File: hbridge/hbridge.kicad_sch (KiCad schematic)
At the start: 81 parts, among them J1 From_MCU, J10 From_MCU, J11 MOSFET_out, J12 Conn_01x03, J13 Conn_01x01_Socket, J14 Conn_01x01_Socket, J15 VEE connector, J16 VEE connector, J17 VEE connector, J18 VEE connector, J2 MOSFET_out, J3 Conn_01x03, J4 From_MCU, J5 MOSFET_out, J6 Conn_01x03, J7 From_MCU, J8 MOSFET_out, J9 Conn_01x03, Q1 IRF3710, Q2 IRF3710, Q3 IRF3710, Q4 IRF3710, U1 LDO-3.3, U5 NSi6651A, U6 NSi6651A, U7 NSi6651A, U8 NSi6651A

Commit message: Half bridge power to PCB added.
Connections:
- net GND_DRV2: no longer J12.2 (Pin_2), J15.1 (Pin_1), J16.1 (Pin_1), J17.1 (Pin_1), J18.1 (Pin_1), J3.2 (Pin_2), J6.2 (Pin_2), J9.2 (Pin_2)
- net +12V: now reaches C3.1, J13.1 (Pin_1), U1.1 (IN)
- net +15_DRV2 renamed +15_DRV2_H
- net +15_DRV2_H: no longer C4.2, C6.2, J12.1 (Pin_1), J6.1 (Pin_1), U6.5 (VCC2), U8.5 (VCC2)
- net -15_DRV2 renamed -15_DRV2_H
- net -15_DRV2_H: no longer J12.3 (Pin_3), J16.3 (Pin_3), J18.3 (Pin_3), J6.3 (Pin_3)
- new net +15_DRV2_L: C4.2, C6.2, J12.1 (Pin_1), J6.1 (Pin_1), U6.5 (VCC2), U8.5 (VCC2)
- new net -15_DRV2_L: J12.3 (Pin_3), J16.3 (Pin_3), J18.3 (Pin_3), J6.3 (Pin_3)
- new net GND_DRV2_H: J15.1 (Pin_1), J17.1 (Pin_1), J3.2 (Pin_2), J9.2 (Pin_2)
- new net GND_DRV2_L: J12.2 (Pin_2), J16.1 (Pin_1), J18.1 (Pin_1), J6.2 (Pin_2)
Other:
- note added: "? мб нужна логика защиты полумоста от мертвого времени и тд?"
- note added: "Q1"
- note added: "Q2"
- note added: "Q3"
- note added: "Q4"
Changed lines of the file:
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@@
 	(generator_version "10.0")
 	(paper "A3")
+	(text "Q1"
+		(exclude_from_sim no)
+		(at 169.418 86.106 0)
+		(effects
+			(font
+				(size 1.27 1.27)
+			)
+		)
+	)
+	(text "Q4"
+		(exclude_from_sim no)
+		(at 358.394 222.758 0)
+		(effects
+			(font
+				(size 1.27 1.27)
+			)
+		)
+	)
+	(text "Q2"
+		(exclude_from_sim no)
+		(at 385.826 102.108 0)
+		(effects
+			(font
+				(size 1.27 1.27)
+			)
+		)
+	)
+	(text "? мб нужна логика защиты полумоста от мертвого времени и тд?"
+		(exclude_from_sim no)
+		(at 72.644 257.302 0)
+		(effects
+			(font
+				(size 1.27 1.27)
+			)
+		)
+	)
+	(text "Q3"
+		(exclude_from_sim no)
+		(at 152.146 186.944 0)
+		(effects
+			(font
+				(size 1.27 1.27)
+			)
+		)
+	)
 	(junction
 		(at 247.65 190.5)
@@
 	)
 	(junction
+		(at 252.73 26.67)
+		(diameter 0)
+		(color 0 0 0 0)
+	)
+	(junction
 		(at 288.29 222.25)
 		(diameter 0)
@@
 	(wire
 		(pts
+			(xy 264.16 25.4) (xy 264.16 26.67)
+		)
+		(stroke
+			(width 0)
+			(type default)
+		)
+	)
+	(wire
+		(pts
 			(xy 257.81 193.04) (xy 257.81 198.12)
 		)
@@
 	(wire
 		(pts
+			(xy 252.73 26.67) (xy 264.16 26.67)
+		)
+		(stroke
+			(width 0)
+			(type default)
+		)
+	)
+	(wire
+		(pts
 			(xy 247.65 207.01) (xy 247.65 210.82)
 		)
@@
 			)
 		)
-		(property "Value" "-15_DRV2"
+		(property "Value" "-15_DRV2_L"
 			(at 284.734 227.838 0)
 			(show_name no)
@@
 			)
 		)
-		(property "Value" "-15_DRV2"
+		(property "Value" "-15_DRV2_H"
 			(at 77.724 191.008 0)
 			(show_name no)
@@
 			)
 		)
-		(property "Value" "-15_DRV2"
+		(property "Value" "-15_DRV2_H"
 			(at 85.09 81.28 0)
 			(show_name no)
@@
 			)
 		)
-		(property "Value" "GND_DRV2"
+		(property "Value" "GND_DRV2_H"
 			(at 98.552 191.008 0)
 			(show_name no)
@@
 			)
 		)
-		(property "Value" "+15_DRV2"
+		(property "Value" "+15_DRV2_H"
 			(at 75.946 158.496 0)
 			(show_name no)
@@
 			)
 		)
-		(property "Value" "GND_DRV2"
+		(property "Value" "GND_DRV2_L"
 			(at 305.562 227.838 0)
 			(show_name no)
@@
 			)
 		)
-		(property "Value" "GND_DRV2"
+		(property "Value" "GND_DRV2_H"
 			(at 109.982 89.408 0)
 			(show_name no)
@@
 	)
 	(symbol
+		(lib_id "power:+12V")
+		(at 264.16 25.4 0)
+		(unit 1)
+		(body_style 1)
+		(exclude_from_sim no)
+		(in_bom yes)
+		(on_board yes)
+		(in_pos_files yes)
+		(dnp no)
+		(fields_autoplaced yes)
+		(property "Reference" "#PWR03"
+			(at 264.16 29.21 0)
+			(hide yes)
+			(show_name no)
+			(do_not_autoplace no)
+			(effects
+				(font
+					(size 1.27 1.27)
+				)
+			)
+		)
+		(property "Value" "+12V"
+			(at 264.16 20.32 0)
+			(show_name no)
+			(do_not_autoplace no)
+			(effects
+				(font
+					(size 1.27 1.27)
+				)
+			)
+		)
+		(property "Footprint" ""
+			(at 264.16 25.4 0)
+			(hide yes)
+			(show_name no)
+			(do_not_autoplace no)
+			(effects
+				(font
+					(size 1.27 1.27)
+				)
+			)
+		)
+		(property "Datasheet" ""
+			(at 264.16 25.4 0)
+			(hide yes)
+			(show_name no)
+			(do_not_autoplace no)
+			(effects
+				(font
+					(size 1.27 1.27)
+				)
+			)
+		)
+		(property "Description" "Power symbol creates a global label with name \"+12V\""
+			(at 264.16 25.4 0)
+			(hide yes)
+			(show_name no)
+			(do_not_autoplace no)
+			(effects
+				(font
+					(size 1.27 1.27)
+				)
+			)
+		)
+		(pin "1"
+		)
+		(instances
+			(project "hbridge"
+				(path "/8009c529-6dc1-42cd-8cc7-a909833d3244"
+					(reference "#PWR03")
+					(unit 1)
+				)
+			)
+		)
+	)
+	(symbol
 		(lib_id "power:+3V3")
 		(at 340.36 63.5 0)
@@
 			)
 		)
-		(property "Value" "GND_DRV2"
+		(property "Value" "GND_DRV2_L"
 			(at 290.322 126.238 0)
 			(show_name no)
@@
 			)
 		)
-		(property "Value" "+15_DRV2"
+		(property "Value" "+15_DRV2_L"
 			(at 267.716 93.726 0)
 			(show_name no)
@@
 			)
 		)
-		(property "Value" "+15_DRV2"
+		(property "Value" "+15_DRV2_L"
 			(at 282.956 195.326 0)
 			(show_name no)
@@
 			)
 		)
-		(property "Value" "+15_DRV2"
+		(property "Value" "+15_DRV2_H"
 			(at 87.376 56.896 0)
 			(show_name no)
@@
 			)
 		)
-		(property "Value" "-15_DRV2"
+		(property "Value" "-15_DRV2_L"
 			(at 269.494 126.238 0)
 			(show_name no)

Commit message: PCB minor changes.
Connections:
- net GND_DRV2: no longer J11.3 (Pin_3), J2.3 (Pin_3), J5.3 (Pin_3), J8.3 (Pin_3), Q1.3 (S), Q2.3 (S), Q3.3 (S), Q4.3 (S), TP11.1, TP3.1, TP5.1, TP8.1
- net GND_DRV2_H: now also J2.3 (Pin_3), J8.3 (Pin_3), Q1.3 (S), Q3.3 (S), TP3.1, TP8.1
- net GND_DRV2_L: now also J11.3 (Pin_3), J5.3 (Pin_3), Q2.3 (S), Q4.3 (S), TP11.1, TP5.1
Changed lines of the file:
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@@
 	)
 	(junction
+		(at 215.9 93.98)
+		(diameter 0)
+		(color 0 0 0 0)
+	)
+	(junction
 		(at 340.36 68.58)
 		(diameter 0)
@@
 	)
 	(junction
+		(at 222.25 195.58)
+		(diameter 0)
+		(color 0 0 0 0)
+	)
+	(junction
 		(at 322.58 67.31)
 		(diameter 0)
@@
 	)
 	(junction
+		(at 21.59 158.75)
+		(diameter 0)
+		(color 0 0 0 0)
+	)
+	(junction
 		(at 331.47 67.31)
 		(diameter 0)
@@
 	)
 	(junction
+		(at 34.29 57.15)
+		(diameter 0)
+		(color 0 0 0 0)
+	)
+	(junction
 		(at 358.14 186.69)
 		(diameter 0)
@@
 	(wire
 		(pts
-			(xy 207.01 195.58) (xy 233.68 195.58)
+			(xy 207.01 195.58) (xy 222.25 195.58)
 		)
 		(stroke
@@
 	(wire
 		(pts
+			(xy 21.59 68.58) (xy 33.02 68.58)
+		)
+		(stroke
+			(width 0)
+			(type default)
+		)
+	)
+	(wire
+		(pts
 			(xy 151.13 162.56) (xy 151.13 163.83)
 		)
@@
 	(wire
 		(pts
+			(xy 21.59 49.53) (xy 21.59 68.58)
+		)
+		(stroke
+			(width 0)
+			(type default)
+		)
+	)
+	(wire
+		(pts
 			(xy 330.2 212.09) (xy 375.92 212.09)
 		)
@@
 	(wire
 		(pts
-			(xy 33.02 57.15) (xy 38.1 57.15)
+			(xy 33.02 57.15) (xy 34.29 57.15)
 		)
 		(stroke
@@
 	(wire
 		(pts
+			(xy 34.29 57.15) (xy 38.1 57.15)
+		)
+		(stroke
+			(width 0)
+			(type default)
+		)
+	)
+	(wire
+		(pts
 			(xy 106.68 80.01) (xy 99.06 80.01)
 		)
@@
 	(wire
 		(pts
+			(xy 231.14 187.96) (xy 222.25 187.96)
+		)
+		(stroke
+			(width 0)
+			(type default)
+		)
+	)
+	(wire
+		(pts
 			(xy 340.36 80.01) (xy 340.36 85.09)
 		)
@@
 	(wire
 		(pts
+			(xy 222.25 187.96) (xy 222.25 195.58)
+		)
+		(stroke
+			(width 0)
+			(type default)
+		)
+	)
+	(wire
+		(pts
 			(xy 160.02 31.75) (xy 171.45 31.75)
 		)
@@
 	(wire
 		(pts
+			(xy 215.9 93.98) (xy 218.44 93.98)
+		)
+		(stroke
+			(width 0)
+			(type default)
+		)
+	)
+	(wire
+		(pts
 			(xy 146.05 44.45) (xy 142.24 44.45)
 		)
@@
 	(wire
 		(pts
+			(xy 21.59 125.73) (xy 21.59 158.75)
+		)
+		(stroke
+			(width 0)
+			(type default)
+		)
+	)
+	(wire
+		(pts
+			(xy 215.9 93.98) (xy 215.9 85.09)
+		)
+		(stroke
+			(width 0)
+			(type default)
+		)
+	)
+	(wire
+		(pts
 			(xy 375.92 212.09) (xy 375.92 189.23)
 		)
@@
 	(wire
 		(pts
+			(xy 231.14 127) (xy 231.14 187.96)
+		)
+		(stroke
+			(width 0)
+			(type default)
+		)
+	)
+	(wire
+		(pts
 			(xy 251.46 35.56) (xy 251.46 38.1)
 		)
@@
 	(wire
 		(pts
+			(xy 33.02 68.58) (xy 33.02 125.73)
+		)
+		(stroke
+			(width 0)
+			(type default)
+		)
+	)
+	(wire
+		(pts
 			(xy 78.74 162.56) (xy 74.93 162.56)
 		)
@@
 	(wire
 		(pts
+			(xy 201.93 127) (xy 231.14 127)
+		)
+		(stroke
+			(width 0)
+			(type default)
+		)
+	)
+	(wire
+		(pts
 			(xy 326.39 77.47) (xy 326.39 81.28)
 		)
@@
 	(wire
 		(pts
+			(xy 201.93 85.09) (xy 201.93 127)
+		)
+		(stroke
+			(width 0)
+			(type default)
+		)
+	)
+	(wire
+		(pts
 			(xy 355.6 186.69) (xy 358.14 186.69)
 		)
@@
 	(wire
 		(pts
+			(xy 222.25 195.58) (xy 233.68 195.58)
+		)
+		(stroke
+			(width 0)
+			(type default)
+		)
+	)
+	(wire
+		(pts
 			(xy 26.67 173.99) (xy 31.75 173.99)
 		)
@@
 	(wire
 		(pts
+			(xy 215.9 85.09) (xy 201.93 85.09)
+		)
+		(stroke
+			(width 0)
+			(type default)
+		)
+	)
+	(wire
+		(pts
 			(xy 289.56 180.34) (xy 302.26 180.34)
 		)
@@
 	(wire
 		(pts
+			(xy 34.29 57.15) (xy 34.29 49.53)
+		)
+		(stroke
+			(width 0)
+			(type default)
+		)
+	)
+	(wire
+		(pts
 			(xy 240.03 40.64) (xy 240.03 38.1)
 		)
@@
 	(wire
 		(pts
+			(xy 34.29 49.53) (xy 21.59 49.53)
+		)
+		(stroke
+			(width 0)
+			(type default)
+		)
+	)
+	(wire
+		(pts
 			(xy 252.73 125.73) (xy 270.51 125.73)
 		)
@@
 	(wire
 		(pts
-			(xy 213.36 93.98) (xy 218.44 93.98)
+			(xy 213.36 93.98) (xy 215.9 93.98)
 		)
 		(stroke
@@
 	(wire
 		(pts
+			(xy 33.02 125.73) (xy 21.59 125.73)
+		)
+		(stroke
+			(width 0)
+			(type default)
+		)
+	)
+	(wire
+		(pts
 			(xy 340.36 68.58) (xy 340.36 72.39)
 		)
@@
 			)
 		)
-		(property "Value" "GND_DRV2"
+		(property "Value" "GND_DRV2_L"
 			(at 238.76 218.694 0)
 			(show_name no)
@@
 			)
 		)
-		(property "Value" "GND_DRV2"
+		(property "Value" "GND_DRV2_H"
 			(at 43.18 80.264 0)
 			(show_name no)
@@
 			)
 		)
-		(property "Value" "GND_DRV2"
+		(property "Value" "GND_DRV2_L"
 			(at 223.52 117.094 0)
 			(show_name no)
@@
 			)
 		)
-		(property "Value" "GND_DRV2"
+		(property "Value" "GND_DRV2_H"
 			(at 31.75 181.864 0)
 			(show_name no)

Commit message: Half-bridge, no MCU.
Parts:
- added J21: Conn_01x01_Socket, Connector:Banana_Jack_1Pin, symbol Connector:Conn_01x01_Socket
- J13, J14: footprint Connector_PinHeader_2.54mm:PinHeader_1x01_P2.54mm_Vertical -> TestPoint:TestPoint_Loop_D1.80mm_Drill1.0mm_Beaded
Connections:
- net drain3 is gone; now on net drain2: J8.2 (Pin_2), Q3.2 (D), R25.1, TP7.1
- net drain2: now also J21.1 (Pin_1)
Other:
- note added: "J13, J14 - просто измерительные точки сначала подразумевалось, что 3.3В можно либо снаружи подать и тогда на J13, J14 перемычки, либо запаять вот это LDO"
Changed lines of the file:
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@@
 		)
 	)
+	(text "J13, J14 - просто измерительные точки\nсначала подразумевалось, что 3.3В можно либо снаружи подать и тогда на J13, J14 перемычки,\nлибо запаять вот это LDO"
+		(exclude_from_sim no)
+		(at 303.022 38.1 0)
+		(effects
+			(font
+				(size 1.27 1.27)
+			)
+		)
+	)
 	(text "Q4"
 		(exclude_from_sim no)
@@
 	)
 	(junction
+		(at 222.25 86.36)
+		(diameter 0)
+		(color 0 0 0 0)
+	)
+	(junction
 		(at 148.59 132.08)
 		(diameter 0)
@@
 		(color 0 0 0 0)
 	)
+	(junction
+		(at 218.44 80.01)
+		(diameter 0)
+		(color 0 0 0 0)
+	)
+	(junction
+		(at 30.48 146.05)
+		(diameter 0)
+		(color 0 0 0 0)
+	)
 	(no_connect
 		(at 314.96 72.39)
@@
 	(wire
 		(pts
+			(xy 30.48 137.16) (xy 48.26 137.16)
+		)
+		(stroke
+			(width 0)
+			(type default)
+		)
+	)
+	(wire
+		(pts
 			(xy 213.36 96.52) (xy 222.25 96.52)
 		)
@@
 	(wire
 		(pts
-			(xy 222.25 96.52) (xy 222.25 81.28)
+			(xy 222.25 96.52) (xy 222.25 86.36)
 		)
 		(stroke
@@
 	(wire
 		(pts
+			(xy 48.26 101.6) (xy 193.04 101.6)
+		)
+		(stroke
+			(width 0)
+			(type default)
+		)
+	)
+	(wire
+		(pts
 			(xy 93.98 41.91) (xy 106.68 41.91)
 		)
@@
 	(wire
 		(pts
-			(xy 30.48 146.05) (xy 40.64 146.05)
-		)
-		(stroke
-			(width 0)
-			(type default)
-		)
-	)
-	(wire
-		(pts
 			(xy 325.12 87.63) (xy 327.66 87.63)
 		)
@@
 	(wire
 		(pts
+			(xy 218.44 80.01) (xy 218.44 86.36)
+		)
+		(stroke
+			(width 0)
+			(type default)
+		)
+	)
+	(wire
+		(pts
 			(xy 375.92 212.09) (xy 375.92 189.23)
 		)
@@
 	(wire
 		(pts
+			(xy 218.44 72.39) (xy 218.44 80.01)
+		)
+		(stroke
+			(width 0)
+			(type default)
+		)
+	)
+	(wire
+		(pts
 			(xy 142.24 30.48) (xy 151.13 30.48)
 		)
@@
 	(wire
 		(pts
+			(xy 193.04 101.6) (xy 193.04 80.01)
+		)
+		(stroke
+			(width 0)
+			(type default)
+		)
+	)
+	(wire
+		(pts
 			(xy 148.59 133.35) (xy 148.59 137.16)
 		)
@@
 	(wire
 		(pts
+			(xy 30.48 137.16) (xy 30.48 146.05)
+		)
+		(stroke
+			(width 0)
+			(type default)
+		)
+	)
+	(wire
+		(pts
 			(xy 257.81 205.74) (xy 257.81 212.09)
 		)
@@
 	(wire
 		(pts
+			(xy 193.04 80.01) (xy 218.44 80.01)
+		)
+		(stroke
+			(width 0)
+			(type default)
+		)
+	)
+	(wire
+		(pts
 			(xy 238.76 210.82) (xy 238.76 213.36)
 		)
@@
 	(wire
 		(pts
+			(xy 48.26 137.16) (xy 48.26 101.6)
+		)
+		(stroke
+			(width 0)
+			(type default)
+		)
+	)
+	(wire
+		(pts
 			(xy 293.37 199.39) (xy 285.75 199.39)
 		)
@@
 	(wire
 		(pts
+			(xy 218.44 86.36) (xy 222.25 86.36)
+		)
+		(stroke
+			(width 0)
+			(type default)
+		)
+	)
+	(wire
+		(pts
 			(xy 285.75 199.39) (xy 281.94 199.39)
 		)
@@
 	(wire
 		(pts
+			(xy 222.25 86.36) (xy 222.25 81.28)
+		)
+		(stroke
+			(width 0)
+			(type default)
+		)
+	)
+	(wire
+		(pts
 			(xy 322.58 81.28) (xy 322.58 85.09)
 		)
@@
 	(wire
 		(pts
+			(xy 30.48 146.05) (xy 40.64 146.05)
+		)
+		(stroke
+			(width 0)
+			(type default)
+		)
+	)
+	(wire
+		(pts
 			(xy 240.03 38.1) (xy 251.46 38.1)
 		)
@@
 			)
 		)
-		(property "Footprint" "Connector_PinHeader_2.54mm:PinHeader_1x01_P2.54mm_Vertical"
+		(property "Footprint" "TestPoint:TestPoint_Loop_D1.80mm_Drill1.0mm_Beaded"
 			(at 227.33 21.59 0)
 			(hide yes)
@@
 			)
 		)
-		(property "Footprint" "Connector_PinHeader_2.54mm:PinHeader_1x01_P2.54mm_Vertical"
+		(property "Footprint" "TestPoint:TestPoint_Loop_D1.80mm_Drill1.0mm_Beaded"
 			(at 252.73 21.59 0)
 			(hide yes)
@@
 					(unit 1)
 				)
+			)
+		)
+	)
+	(symbol
+		(lib_id "Connector:Conn_01x01_Socket")
+		(at 223.52 72.39 0)
+		(unit 1)
+		(body_style 1)
+		(exclude_from_sim no)
+		(in_bom yes)
+		(on_board yes)
+		(in_pos_files yes)
+		(dnp no)
+		(fields_autoplaced yes)
+		(property "Reference" "J21"
+			(at 224.79 71.1199 0)
+			(show_name no)
+			(do_not_autoplace no)
+			(effects
+				(font
+					(size 1.27 1.27)
+				)
+				(justify left)
+			)
+		)
+		(property "Value" "Conn_01x01_Socket"
+			(at 224.79 73.6599 0)
+			(show_name no)
+			(do_not_autoplace no)
+			(effects
+				(font
+					(size 1.27 1.27)
+				)
+				(justify left)
+			)
+		)
+		(property "Footprint" "Connector:Banana_Jack_1Pin"
+			(at 223.52 72.39 0)
+			(hide yes)
+			(show_name no)
+			(do_not_autoplace no)
+			(effects
+				(font
+					(size 1.27 1.27)
+				)
+			)
+		)
+		(property "Datasheet" ""
+			(at 223.52 72.39 0)
+			(hide yes)
+			(show_name no)
+			(do_not_autoplace no)
+			(effects
+				(font
+					(size 1.27 1.27)
+				)
+			)
+		)
+		(property "Description" "Generic connector, single row, 01x01, script generated"
+			(at 223.52 72.39 0)
+			(hide yes)
+			(show_name no)
+			(do_not_autoplace no)
+			(effects
+				(font
+					(size 1.27 1.27)
+				)
+			)
+		)
+		(pin "1"
+		)
+		(instances
+			(project "hbridge"
+				(path "/8009c529-6dc1-42cd-8cc7-a909833d3244"
+					(reference "J21")
+					(unit 1)
+				)

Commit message: Hierarchy changed. MCU optocouplers started.
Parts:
- renumbered C4 to C12, C6 to C13, C5 to C7, C2 to C8, D13 to D1, D11 to D19, D10 to D2, D16 to D20, D9 to D21, D12 to D22, D17 to D23, D18 to D24, D14 to D3, D8 to D4, D15 to D5, D7 to D6, Q3 to Q5, Q1 to Q6, Q2 to Q7, Q4 to Q8, R25 to R1, R30 to R10, R14 to R11, R15 to R12, R26 to R2, R27 to R3, R19 to R37, R20 to R38, R21 to R39, R16 to R4, R31 to R40, R32 to R41, R33 to R42, R22 to R43, R23 to R44, R34 to R45, R24 to R46, R35 to R47, R36 to R48, R17 to R5, R18 to R6, R28 to R7, R29 to R8, R13 to R9, TP7 to TP13, TP8 to TP14, TP9 to TP15, TP2 to TP16, TP3 to TP17, TP1 to TP18, TP4 to TP19, TP5 to TP20, TP6 to TP21, TP10 to TP22, TP11 to TP23, TP12 to TP24, U6 to U11, U8 to U12, U7 to U2, U5 to U3
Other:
- note added: "надо сделать оптопары для мк и connector 4 входа на каждый ключ = 16. Так как будут оптопары, согласования по питанию нет."

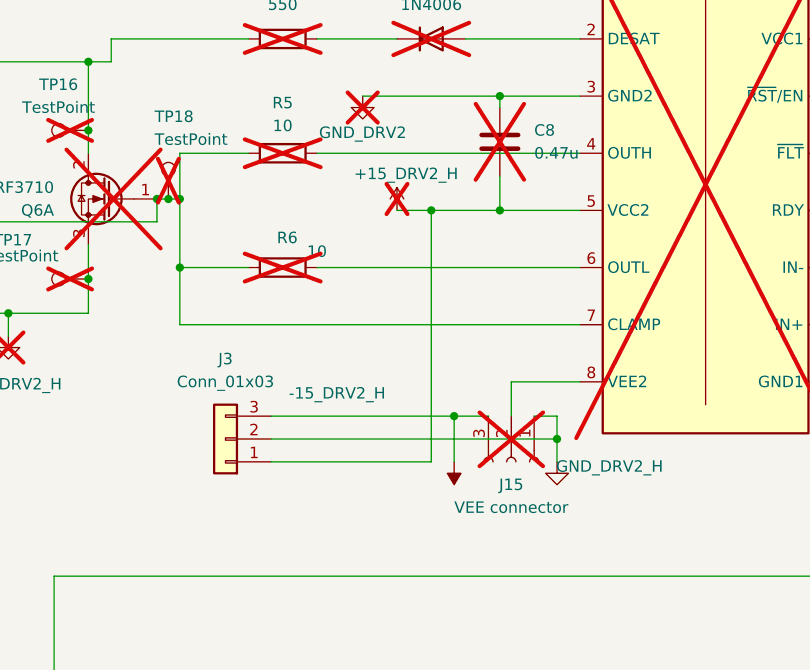
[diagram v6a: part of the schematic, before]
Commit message: Half-bridge refactoring start.
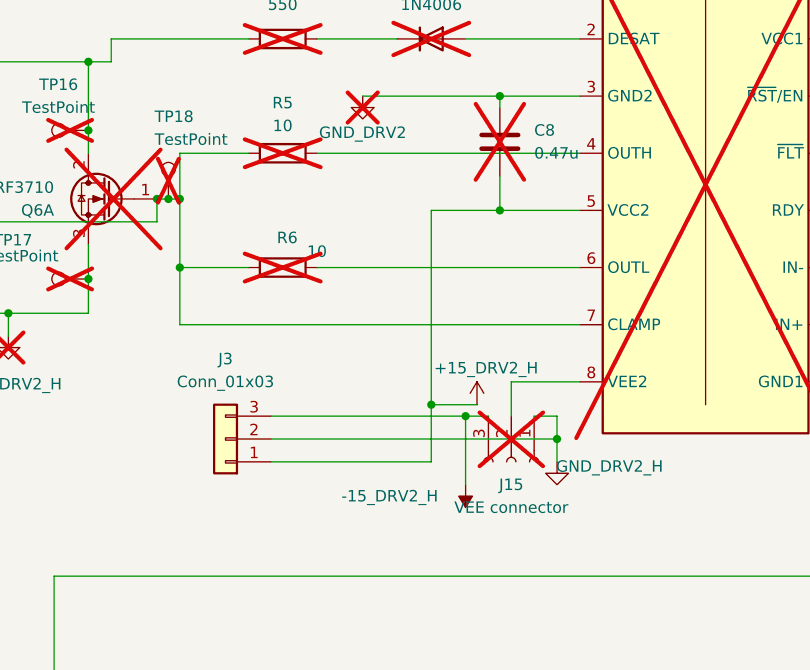
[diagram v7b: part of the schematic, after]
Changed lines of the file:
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@@
 	)
 	(junction
+		(at 90.17 82.55)
+		(diameter 0)
+		(color 0 0 0 0)
+	)
+	(junction
 		(at 391.16 184.15)
 		(diameter 0)
@@
 	)
 	(junction
+		(at 93.98 83.82)
+		(diameter 0)
+		(color 0 0 0 0)
+	)
+	(junction
 		(at 186.69 144.78)
 		(diameter 0)
@@
 	)
 	(junction
-		(at 90.17 60.96)
-		(diameter 0)
-		(color 0 0 0 0)
-	)
-	(junction
 		(at 238.76 210.82)
 		(diameter 0)
@@
 	)
 	(junction
-		(at 92.71 83.82)
-		(diameter 0)
-		(color 0 0 0 0)
-	)
-	(junction
 		(at 251.46 26.67)
 		(diameter 0)
@@
 	(wire
 		(pts
+			(xy 90.17 82.55) (xy 90.17 88.9)
+		)
+		(stroke
+			(width 0)
+			(type default)
+		)
+	)
+	(wire
+		(pts
 			(xy 104.14 86.36) (xy 104.14 88.9)
 		)
@@
 	(wire
 		(pts
-			(xy 72.39 83.82) (xy 92.71 83.82)
+			(xy 72.39 83.82) (xy 93.98 83.82)
 		)
 		(stroke
@@
 	(wire
 		(pts
-			(xy 90.17 88.9) (xy 90.17 60.96)
+			(xy 90.17 60.96) (xy 90.17 82.55)
 		)
 		(stroke
@@
 	(wire
 		(pts
-			(xy 90.17 60.96) (xy 86.36 60.96)
+			(xy 90.17 82.55) (xy 95.25 82.55)
 		)
 		(stroke
@@
 	(wire
 		(pts
-			(xy 92.71 83.82) (xy 92.71 88.9)
+			(xy 93.98 83.82) (xy 93.98 91.44)
 		)
 		(stroke
@@
 	(wire
 		(pts
-			(xy 96.52 83.82) (xy 92.71 83.82)
+			(xy 96.52 83.82) (xy 93.98 83.82)
 		)
 		(stroke
@@
 	(symbol
 		(lib_id "power:-24V")
-		(at 92.71 88.9 0)
+		(at 93.98 91.44 0)
 		(mirror x)
 		(unit 1)
@@
 		(dnp no)
 		(property "Reference" "#PWR065"
-			(at 92.71 85.09 0)
+			(at 93.98 87.63 0)
 			(hide yes)
 			(show_name no)
@@
 		)
 		(property "Value" "-15_DRV2_H"
-			(at 85.09 81.28 0)
+			(at 90.932 92.71 0)
 			(show_name no)
 			(do_not_autoplace no)
@@
 		)
 		(property "Footprint" ""
-			(at 92.71 88.9 0)
+			(at 93.98 91.44 0)
 			(hide yes)
 			(show_name no)
@@
 		)
 		(property "Datasheet" ""
-			(at 92.71 88.9 0)
+			(at 93.98 91.44 0)
 			(hide yes)
 			(show_name no)
@@
 		)
 		(property "Description" "Power symbol creates a global label with name \"-24V\""
-			(at 92.71 88.9 0)
+			(at 93.98 91.44 0)
 			(hide yes)
 			(show_name no)
@@
 	(symbol
 		(lib_id "power:+3V3")
-		(at 86.36 60.96 0)
+		(at 95.25 82.55 0)
 		(unit 1)
 		(body_style 1)
-		(exclude_from_sim yes)
-		(in_bom no)
-		(on_board no)
+		(exclude_from_sim no)
+		(in_bom yes)
+		(on_board yes)
 		(in_pos_files yes)
-		(dnp yes)
+		(dnp no)
 		(property "Reference" "#PWR090"
-			(at 86.36 64.77 0)
+			(at 95.25 86.36 0)
 			(hide yes)
 			(show_name no)
@@
 		)
 		(property "Value" "+15_DRV2_H"
-			(at 87.376 56.896 0)
+			(at 96.266 78.486 0)
 			(show_name no)
 			(do_not_autoplace no)
@@
 		)
 		(property "Footprint" ""
-			(at 86.36 60.96 0)
+			(at 95.25 82.55 0)
 			(hide yes)
 			(show_name no)
@@
 		)
 		(property "Datasheet" ""
-			(at 86.36 60.96 0)
+			(at 95.25 82.55 0)
 			(hide yes)
 			(show_name no)
@@
 		)
 		(property "Description" "Power symbol creates a global label with name \"+3V3\""
-			(at 86.36 60.96 0)
+			(at 95.25 82.55 0)
 			(hide yes)
 			(show_name no)
